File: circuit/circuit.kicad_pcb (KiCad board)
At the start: 2 copper layers, 188.2 x 119.6 mm, 199 parts, among them J201 Barrel_Jack, J301 FX_R_2, J302 FX_R_4, J303 FX_R_56, J304 FX_R_8, J305 FX_R_1, J306 FX_R_3, J307 FX_R_5, J308 FX_R_7, J309 FX_S_1, J310 FX_S_2, J311 FX_S_3, J312 FX_S_4, J313 FX_S_5, J314 FX_S_6, J315 FX_S_7, J316 FX_S_8, J317 Guitar_In, J318 Amp_Out, SW101 Pedal_1, SW102 Pedal_2, SW103 Pedal_3, SW104 Pedal_4, SW105 Pedal_5, SW106 Pedal_6, SW107 Pedal_7, SW108 Pedal_8, SW109 Program, SW110 Preset, U101 ESP32-S3-DevKitC, U16 CD4051B, U201 TMA-1215D, U202 LM7805_TO220, U203 LM7905_TO220, U204 AMS1117-3.3, U301 TL072, U302 TL072, U303 TL072, U304 TL072, U305 TL072, U306 TL072, U307 TL072, U308 TL072, U309 TL072, U401 ADG419BN, U402 CD4051B, U501 CD4051B, U502 CD4051B, U503 CD4051B, U504 CD4051B, U601 CD4051B, U602 CD4051B, U603 CD4051B, U604 CD4051B, U701 74HC595, U702 74HC595, U703 74HC595, U704 74HC595, U801 74HC595, U802 74HC595, U901 74HC595, U902 74HC595

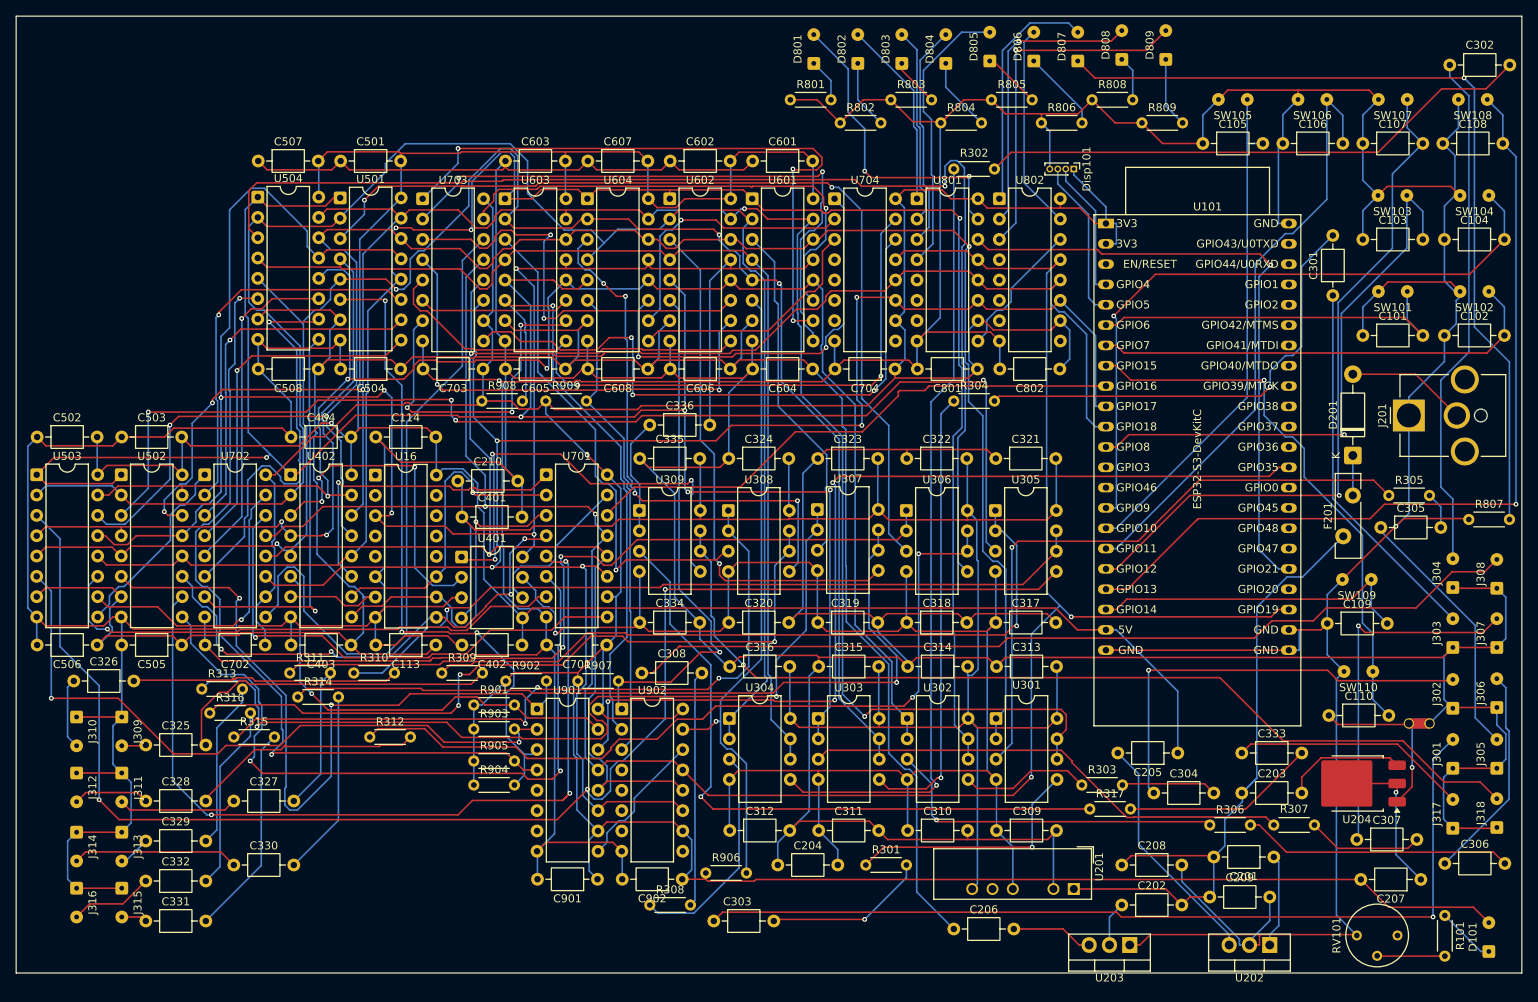
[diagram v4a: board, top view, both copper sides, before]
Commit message: Fine tuning of circuit
Added jumper to select voltage of display, changed 3.3V regulator from SMD to TO-220 to simplify DIY builds.
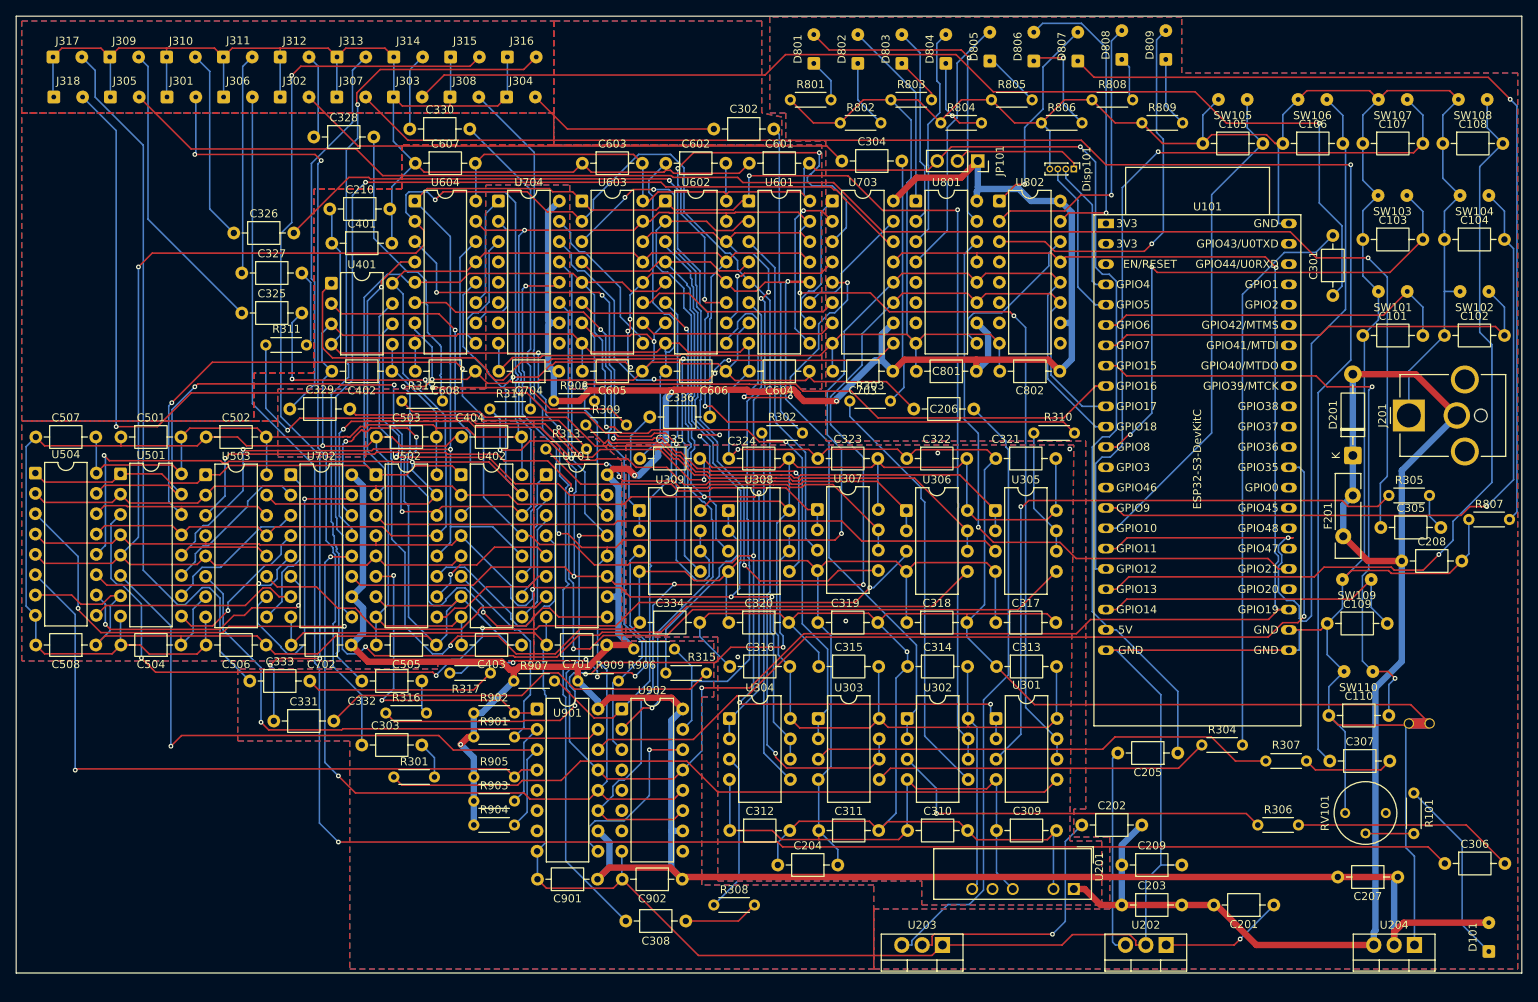
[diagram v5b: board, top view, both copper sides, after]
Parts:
- removed C113, C114: 0.1uF, Capacitor_THT:C_Axial_L3.8mm_D2.6mm_P7.50mm_Horizontal
- removed U16: CD4051B, Package_DIP:CERDIP-16_W7.62mm_SideBrazed
- added JP101: Jumper_3_Open, Connector_PinSocket_2.54mm:PinSocket_1x03_P2.54mm_Vertical, F.Cu at (171.0, 51.0)
- J303: value FX_R_56 -> FX_R_6
- U204: value AMS1117-3.3 -> LM1117T-3.3; footprint Package_TO_SOT_SMD:TO-252-3_TabPin2 -> Package_TO_SOT_THT:TO-220-3_Vertical
- moved J318 202.2 mm to (55.5, 43.0), turned to 0 degrees
- moved J317 199.8 mm to (55.4, 38.0), turned to 0 degrees
- moved J305 192.6 mm to (62.6, 43.0), turned to 0 degrees
- moved J301 181.3 mm to (69.7, 43.0), turned to 0 degrees
- moved J306 176.5 mm to (76.7, 43.0), turned to 0 degrees
- moved J302 165.3 mm to (83.8, 43.0), turned to 0 degrees
- moved J307 160.5 mm to (90.9, 43.0), turned to 0 degrees
- moved J303 149.2 mm to (98.0, 43.0), turned to 0 degrees
- moved J308 144.5 mm to (105.0, 43.0), turned to 0 degrees
- moved J304 133.2 mm to (112.1, 43.0), turned to 0 degrees
- moved C333 124.3 mm to (80.0, 116.0)
- moved J316 117.0 mm to (112.2, 38.0), turned to 0 degrees
- moved J315 111.7 mm to (105.1, 38.0), turned to 0 degrees
- moved J314 104.7 mm to (98.0, 38.0), turned to 0 degrees
- moved J313 100.6 mm to (90.9, 38.0), turned to 0 degrees
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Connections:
- C203 pad 2: Net-(U204-VI) -> VIN_12V
- C207 pad 1: Net-(U204-VO) -> 3.3V
- D201 pad 1: Net-(D201-K) -> VIN_12V
- D201 pad 2: Net-(D201-A) -> VIN_12V
- Disp101 pad 1: 3.3V -> Net-(Disp101-VCC)
- F201 pad 2: Net-(D201-K) -> VIN_12V
- J201 pad 2: Net-(D201-A) -> VIN_12V
- U101 pad 1: 3.3V -> unconnected-(U101-3V3-Pad1)_1
- U101 pad 2: 3.3V -> unconnected-(U101-3V3-Pad1)
- U204 pad 2: Net-(U204-VO) -> 3.3V
- U204 pad 3: Net-(U204-VI) -> VIN_12V
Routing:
- net Net-(C306-Pad1): track 27.3 -> 237.0 mm, vias 0 -> 1
- net Net-(C305-Pad1): track 32.5 -> 196.9 mm, vias 0 -> 1
- net Net-(C307-Pad1): track 45.2 -> 203.4 mm
- net Net-(C331-Pad1): track 3.21 -> 113.6 mm, vias 0 -> 3
- net /IO Routing/U7_Q5: track 114.3 -> 17.3 mm, vias 3 -> 1
- net Net-(C301-Pad1): track 46.6 -> 141.1 mm, vias 0 -> 1
- net Net-(C326-Pad2): track 33.7 -> 127.9 mm, vias 0 -> 2
- net Net-(C332-Pad1): track 10.5 -> 101.4 mm, vias 0 -> 1
- net GUITAR_IN: track 242.9 -> 156.3 mm, vias 5 -> 0
- net Net-(U305-2-): track 97.4 -> 15.9 mm, vias 1 -> 0
- net VIN_12V: track 86.1 -> 166.1 mm
- net -5V: track 312.8 -> 238.2 mm, vias 0 -> 3
- net /IO Routing/U7_Q6: track 90.0 -> 15.8 mm, vias 2 -> 0
- net Net-(U307-1-): track 111.7 -> 40.0 mm, vias 2 -> 0
- net AGND: track 801.4 -> 730.6 mm, vias 0 -> 7
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- added copper zone on B.Cu, net AGND
- added copper zone on F.Cu, net AGND
- added copper zone on B.Cu, net GND
- added copper zone on F.Cu, net GND

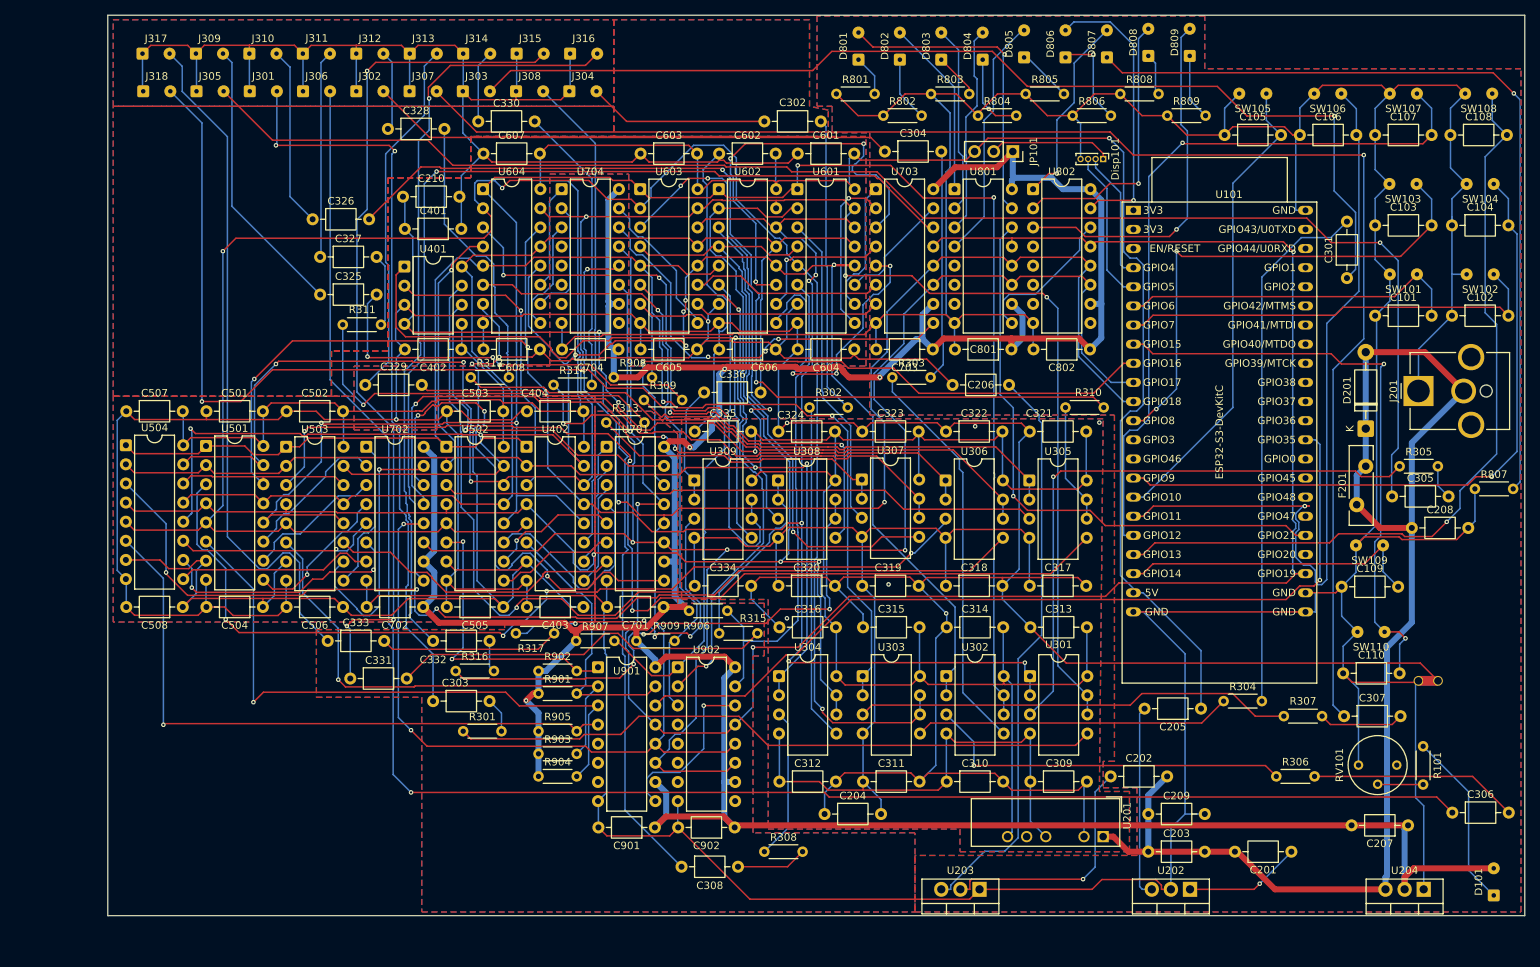
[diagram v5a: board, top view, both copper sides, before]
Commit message: Added ferrite beads and tweaked PCB
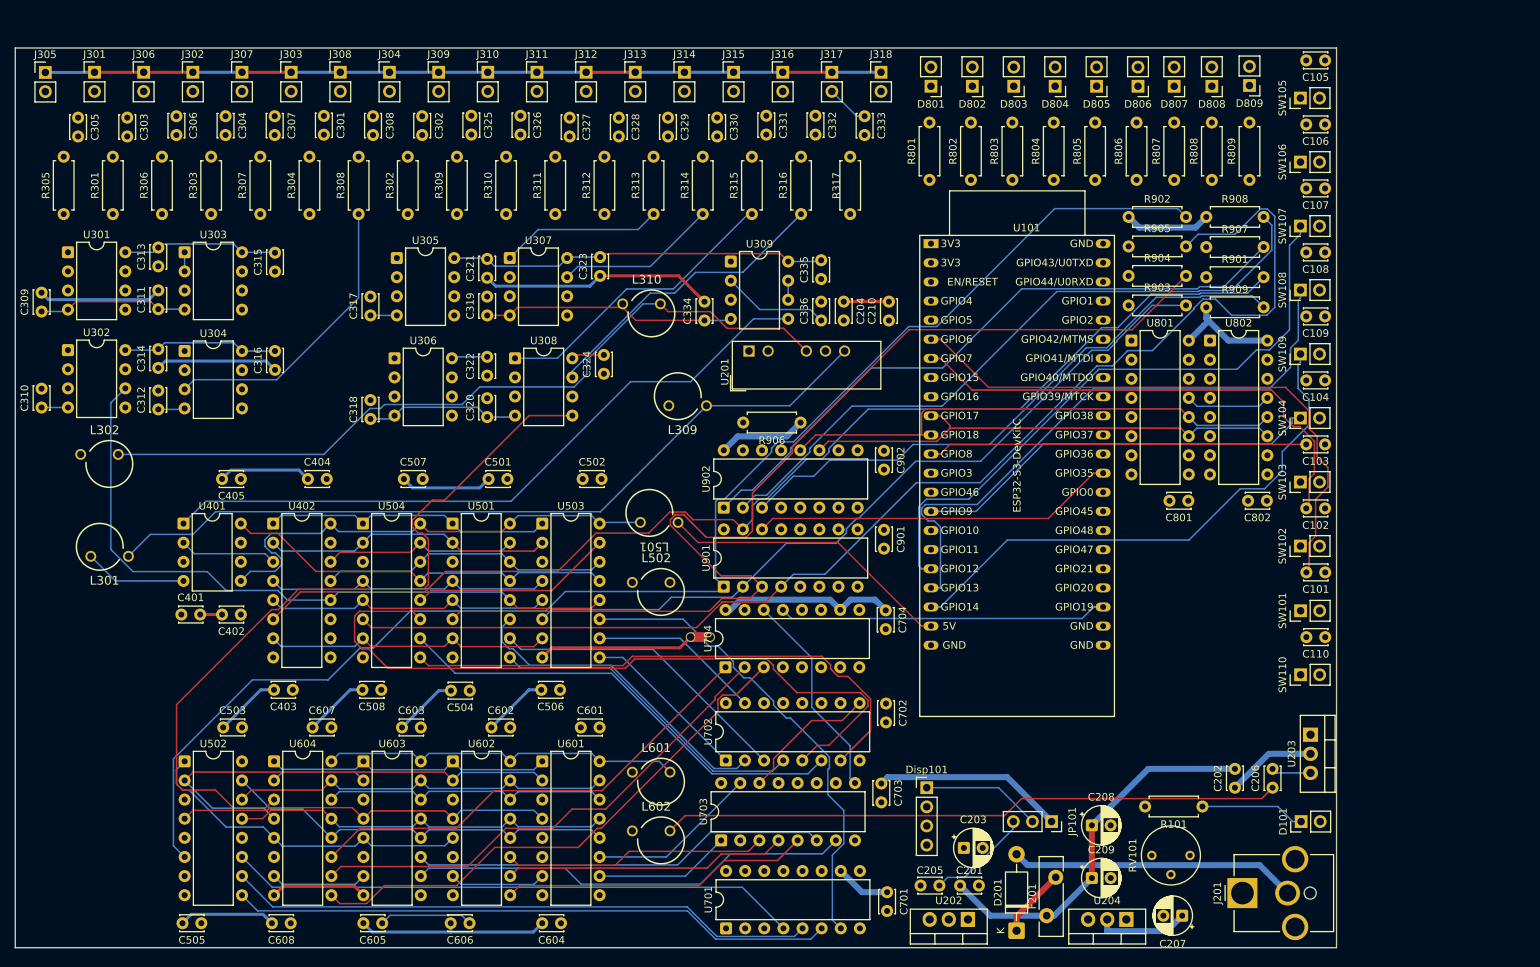
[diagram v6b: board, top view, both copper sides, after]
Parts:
- added C405: 0.1uF, Capacitor_THT:C_Disc_D3.0mm_W2.0mm_P2.50mm, F.Cu at (68.5, 94.5)
- added L301: 600R@100Mhz, WE-UKW:WE-UKW_74275010, F.Cu at (49.7, 103.5)
- added L302: 600R@100Mhz, WE-UKW:WE-UKW_74275010, F.Cu at (51.0, 92.5)
- added L309: 600R@100Mhz, WE-UKW:WE-UKW_74275010, F.Cu at (126.5, 83.5)
- added L310: 600R@100Mhz, WE-UKW:WE-UKW_74275010, F.Cu at (123.0, 72.5)
- added L501: 600R@100Mhz, WE-UKW:WE-UKW_74275010, F.Cu at (122.7, 99.0)
- added L502: 600R@100Mhz, WE-UKW:WE-UKW_74275010, F.Cu at (124.3, 109.5)
- added L601: 600R@100Mhz, WE-UKW:WE-UKW_74275010, F.Cu at (124.3, 134.7)
- added L602: 600R@100Mhz, WE-UKW:WE-UKW_74275010, F.Cu at (124.3, 142.5)
- C101, C102, C103, C104, C105, C106, C107, C108, C109, C110, C201, C202, C204, C205, C206, C210, C301, C302, C303, C304, C305, C306, C307, C308, C309, C310, C311, C312, C313, C314, C315, C316, C317, C318, C319, C320, C321, C322, C323, C324, C325, C326, C327, C328, C329, C330, C331, C332, C333, C334, C335, C336, C401, C402, C403, C404, C501, C502, C503, C504, C505, C506, C507, C508, C601, C602, C603, C604, C605, C606, C607, C608, C701, C702, C703, C704, C801, C802, C901, C902: footprint Capacitor_THT:C_Axial_L3.8mm_D2.6mm_P7.50mm_Horizontal -> Capacitor_THT:C_Disc_D3.0mm_W2.0mm_P2.50mm
- C203, C207, C208, C209: footprint Capacitor_THT:C_Axial_L3.8mm_D2.6mm_P7.50mm_Horizontal -> Capacitor_THT:CP_Radial_D5.0mm_P2.50mm
- D101, D801, D802, D803, D804, D805, D806, D807, D808, D809, SW101, SW102, SW103, SW104, SW105, SW106, SW107, SW108, SW109, SW110: footprint Connector_Wire:SolderWire-0.1sqmm_1x02_P3.6mm_D0.4mm_OD1mm -> Connector_PinHeader_2.54mm:PinHeader_1x02_P2.54mm_Vertical
- Disp101: footprint Connector_PinHeader_1.00mm:PinHeader_1x04_P1.00mm_Vertical -> Connector_PinHeader_2.54mm:PinHeader_1x04_P2.54mm_Vertical
- J301, J302, J303, J304, J305, J306, J307, J308, J309, J310, J311, J312, J313, J314, J315, J316, J317, J318: footprint Bay:Pedal_Jack -> Library:Jack
- R101, R301, R302, R303, R304, R305, R306, R307, R308, R309, R310, R311, R312, R313, R314, R315, R316, R317, R801, R802, R803, R804, R805, R806, R807, R808, R809, R901, R902, R903, R904, R905, R906, R907, R908, R909: footprint Resistor_THT:R_Axial_DIN0204_L3.6mm_D1.6mm_P5.08mm_Horizontal -> Resistor_THT:R_Axial_DIN0207_L6.3mm_D2.5mm_P7.62mm_Horizontal
- U301, U302, U303, U304, U305, U306, U307, U308, U309: footprint Package_DIP:CERDIP-8_W7.62mm_SideBrazed -> Package_DIP:DIP-8_W7.62mm
- U402, U501, U502, U503, U504, U601, U602, U603, U604, U701, U702, U703, U704, U801, U802, U901, U902: footprint Package_DIP:CERDIP-16_W7.62mm_SideBrazed -> Package_DIP:DIP-16_W7.62mm
- moved C306 193.1 mm to (59.9, 46.3), turned to -90 degrees
- moved C305 181.6 mm to (46.8, 46.5), turned to -90 degrees
- moved R305 180.6 mm to (44.9, 59.3), turned to 90 degrees
- moved R306 165.8 mm to (58.0, 59.3), turned to 90 degrees
- moved C307 162.9 mm to (73.0, 46.3), turned to -90 degrees
- moved R307 151.4 mm to (71.1, 59.3), turned to 90 degrees
- moved C309 145.4 mm to (42.0, 72.2), turned to 90 degrees
- moved U301 139.6 mm to (45.5, 64.4)
- moved C301 137.6 mm to (79.5, 46.3), turned to -90 degrees
- moved R304 137.6 mm to (77.6, 59.3), turned to 90 degrees
- moved C310 130.1 mm to (42.0, 85.0), turned to 90 degrees
- moved C313 125.4 mm to (57.5, 66.2), turned to 90 degrees
- moved U302 124.4 mm to (45.5, 77.4)
- moved C311 112.7 mm to (57.5, 71.9), turned to 90 degrees
- moved C314 110.2 mm to (57.5, 79.8), turned to 90 degrees
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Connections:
- net Net-(U202-VI) renamed /Power/12V_to_5V
- net Net-(U203-VI) renamed /Power/12V_to_-5V
- C203 pad 2: VIN_12V -> /Power/12V_to_3.3V
- C207 pad 1: 3.3V -> /Power/3.3V_1
- C309 pad 1: -15V -> _15V_F
- C310 pad 1: -15V -> _15V_F
- C311 pad 1: -15V -> _15V_F
- C312 pad 1: -15V -> _15V_F
- C313 pad 2: +15V -> +15V_F
- C314 pad 2: +15V -> +15V_F
- C315 pad 2: +15V -> +15V_F
- C316 pad 2: +15V -> +15V_F
- C317 pad 1: -15V -> Net-(U305-V-)
- C318 pad 1: -15V -> Net-(U305-V-)
- C319 pad 1: -15V -> Net-(U305-V-)
- C320 pad 1: -15V -> Net-(U305-V-)
- C321 pad 2: +15V -> Net-(U305-V+)
- C322 pad 2: +15V -> Net-(U305-V+)
- C323 pad 2: +15V -> Net-(U305-V+)
- C324 pad 2: +15V -> Net-(U305-V+)
- C334 pad 1: -15V -> Net-(U305-V-)
- C335 pad 2: +15V -> Net-(U305-V+)
- C401 pad 1: +15V -> +15V_F
- C402 pad 1: +5V -> +5V_F
- C403 pad 1: -5V -> -5V_F
- C404 pad 2: +5V -> +5V_F
- C501 pad 2: +5V -> +5V_F
- C502 pad 2: +5V -> +5V_F
- C503 pad 2: +5V -> +5V_F
- C504 pad 1: -5V -> -5V_F
- C505 pad 1: -5V -> -5V_F
- C506 pad 1: -5V -> -5V_F
- C507 pad 2: +5V -> +5V_F
- C508 pad 1: -5V -> -5V_F
- C601 pad 2: +5V -> Net-(U601-VDD)
- C602 pad 2: +5V -> Net-(U601-VDD)
- C603 pad 2: +5V -> Net-(U601-VDD)
- C604 pad 1: -5V -> Net-(U601-VEE)
- C605 pad 1: -5V -> Net-(U601-VEE)
- C606 pad 1: -5V -> Net-(U601-VEE)
- C607 pad 2: +5V -> Net-(U601-VDD)
- C608 pad 1: -5V -> Net-(U601-VEE)
- D201 pad 1: VIN_12V -> /Power/12V_RAW_2
- D201 pad 2: VIN_12V -> /Power/12V_RAW_1
- F201 pad 2: VIN_12V -> /Power/12V_RAW_2
- J201 pad 2: VIN_12V -> /Power/12V_RAW_1
- U204 pad 2: 3.3V -> /Power/3.3V_1
- U204 pad 3: VIN_12V -> /Power/12V_to_3.3V
- U301 pad 4: -15V -> _15V_F
- U301 pad 8: +15V -> +15V_F
- U302 pad 4: -15V -> _15V_F
- U302 pad 8: +15V -> +15V_F
- U303 pad 4: -15V -> _15V_F
- U303 pad 8: +15V -> +15V_F
- U304 pad 4: -15V -> _15V_F
- U304 pad 8: +15V -> +15V_F
- U305 pad 4: -15V -> Net-(U305-V-)
- U305 pad 8: +15V -> Net-(U305-V+)
- U306 pad 4: -15V -> Net-(U305-V-)
- U306 pad 8: +15V -> Net-(U305-V+)
- U307 pad 4: -15V -> Net-(U305-V-)
- U307 pad 8: +15V -> Net-(U305-V+)
- U308 pad 4: -15V -> Net-(U305-V-)
- U308 pad 8: +15V -> Net-(U305-V+)
- U309 pad 4: -15V -> Net-(U305-V-)
- U309 pad 8: +15V -> Net-(U305-V+)
- U401 pad 4: +15V -> +15V_F
- U401 pad 5: +5V -> +5V_F
- U401 pad 7: -15V -> -15V_F
- U402 pad 16: +5V -> +5V_F
- U402 pad 7: -5V -> -5V_F
- U501 pad 16: +5V -> +5V_F
- U501 pad 7: -5V -> -5V_F
- U502 pad 16: +5V -> +5V_F
- U502 pad 7: -5V -> -5V_F
- U503 pad 16: +5V -> +5V_F
- U503 pad 7: -5V -> -5V_F
- U504 pad 16: +5V -> +5V_F
- U504 pad 7: -5V -> -5V_F
- U601 pad 16: +5V -> Net-(U601-VDD)
- U601 pad 7: -5V -> Net-(U601-VEE)
- U602 pad 16: +5V -> Net-(U601-VDD)
- U602 pad 7: -5V -> Net-(U601-VEE)
- U603 pad 16: +5V -> Net-(U601-VDD)
- U603 pad 7: -5V -> Net-(U601-VEE)
- U604 pad 16: +5V -> Net-(U601-VDD)
- U604 pad 7: -5V -> Net-(U601-VEE)
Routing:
- net GND: track 672.8 -> 0.00 mm
- net Net-(C306-Pad1): track 237.0 -> 5.71 mm, vias 1 -> 0
- net Net-(C307-Pad1): track 203.4 -> 5.71 mm, vias 1 -> 0
- net +5V: track 313.1 -> 120.1 mm, vias 1 -> 0
- net Net-(C305-Pad1): track 196.9 -> 5.78 mm, vias 1 -> 0
- net SR_OE: track 312.3 -> 147.9 mm, vias 5 -> 0
- net +15V: track 269.6 -> 114.0 mm, vias 3 -> 0
- net /IO Routing/U901_Q1: track 38.0 -> 187.3 mm, vias 2 -> 0
- net -15V: track 252.5 -> 110.0 mm, vias 1 -> 0
- net /Inhibit Registers/U902_Q3: track 81.3 -> 218.0 mm, vias 1 -> 0
- net Net-(C301-Pad1): track 141.1 -> 5.69 mm, vias 1 -> 0
- net -5V_F: track 0.00 -> 134.7 mm
- net SR_STCP: track 262.8 -> 128.5 mm, vias 5 -> 0
- net Net-(C326-Pad2): track 127.9 -> 3.73 mm, vias 2 -> 0
- net -5V: track 238.2 -> 116.2 mm, vias 3 -> 0
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- added copper zone on In2.Cu, net GND
- removed copper zone on B.Cu, net AGND
- removed copper zone on F.Cu, net AGND
- removed copper zone on B.Cu, net GND
- removed copper zone on F.Cu, net GND
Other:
- board size 188.2 x 119.6 mm -> 175.5 x 119.5 mm
- copper layers 2 -> 4
